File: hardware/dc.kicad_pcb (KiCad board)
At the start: 4 copper layers, 40 x 40 mm, 92 parts, among them J1 DRILL, J2 DRILL, J3 DRILL, J4 DRILL, J5 USB-MINI-B-SMD, J6 STACK-UP-HIGH, J7 STACK-DOWN, J8 STACK-UP-HIGH, J9 STACK-DOWN, P1 black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

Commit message: Add 3d information (tbc); fix direction of some diodes
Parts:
- C1, C12, C13, C14, C16, C17, C18, C19, C2, C20, C22, C24, C25, C9, FB1, FB2, FB3, FB4, FB5: footprint 0402 -> C0402
- C10, C21, C8, L2: footprint 0805 -> C0805
- C11, C15, C23, C5, C6, R9: footprint 0603 -> C0603
- C3, C4: footprint kicad-libraries:ELKO_83 -> ELKO_83
- C7: footprint kicad-libraries:3528-21 -> 3528-21
- D1, D2: footprint kicad-libraries:D0603 -> D0603
- D3, D6, D7, D8, D9: footprint kicad-libraries:SOD-123 -> SOD-123
- D4, D5: footprint kicad-libraries:SOD-128 -> SOD-128
- J5: footprint kicad-libraries:USB-MINI-B-SMD -> USB-MINI-B-SMD
- J6, J8: footprint kicad-libraries:BTB08-ACS-TOP -> BTB08-ACS-TOP
- J7, J9: footprint kicad-libraries:BTB08-ACS-BTM -> BTB08-ACS-BTM
- L1: footprint kicad-libraries:NR3030 -> NR3030
- P1, P2: footprint kicad-libraries:OQ_2P -> OQ_2P
- P3, P4: footprint kicad-libraries:CON-SENSOR -> CON-SENSOR
- Q1, Q2: footprint kicad-libraries:SOIC-8-MOSFET -> SOIC-8-MOSFET
- R1, R10, R11, R12, R13, R15, R18, R2, R3, R4, R5, R6, R7, R8: footprint 0402 -> R0402
- R14: footprint 1206 -> R1206
- R16, R17: footprint 0603 -> R0603
- RP1, RP2, RP3, RP4: footprint kicad-libraries:741X083 -> 4X0402
- SW1, SW2: footprint kicad-libraries:TACT-SWITCH -> TACT-SWITCH
- U1: footprint kicad-libraries:LQFP64 -> LQFP64
- U2: footprint kicad-libraries:PQFN-32 -> PQFN-32
- X1: footprint kicad-libraries:CRYSTAL_3225 -> CRYSTAL_3225
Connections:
- J5 pad 4: (no net) -> Net-(J5-Pad4)
- RP1 pad 2: (no net) -> Net-(RP1-Pad2)
- RP1 pad 3: (no net) -> Net-(RP1-Pad3)
- RP1 pad 6: (no net) -> Net-(RP1-Pad6)
- RP1 pad 7: (no net) -> Net-(RP1-Pad7)
- RP4 pad 6: (no net) -> Net-(RP4-Pad6)
- RP4 pad 7: (no net) -> Net-(RP4-Pad7)
- U1 pad 25: (no net) -> Net-(U1-Pad25)
- U1 pad 31: (no net) -> Net-(U1-Pad31)
- U1 pad 32: (no net) -> Net-(U1-Pad32)
- U1 pad 40: (no net) -> Net-(U1-Pad40)
- U1 pad 50: (no net) -> Net-(U1-Pad50)
- U1 pad 52: (no net) -> Net-(U1-Pad52)
- U2 pad 9: (no net) -> Net-(U2-Pad9)

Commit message: Add 3d information (final)
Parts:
- added REF**: heatsink, kicad-libraries:heatsink, F.Cu at (150.8, 95.0)
- Q3: footprint SOT23GDS -> kicad-libraries:SOT23GDS
- U2: footprint PQFN-32 -> kicad-libraries:PQFN-32

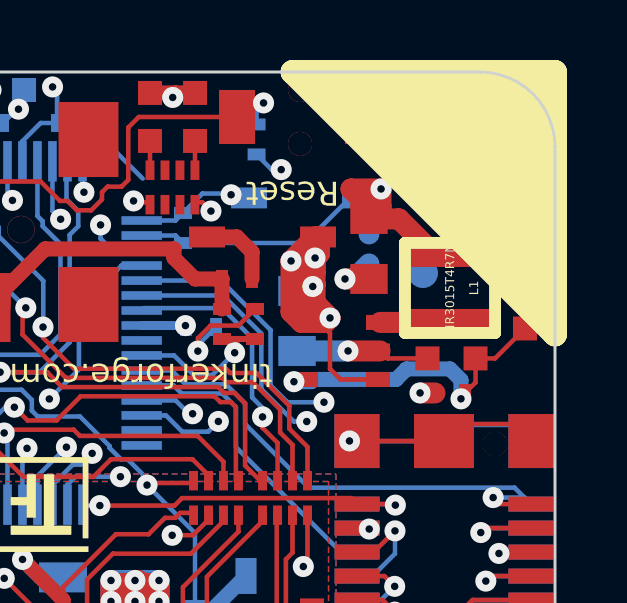
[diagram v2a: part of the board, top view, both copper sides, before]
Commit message: Add 3d component: NR3030
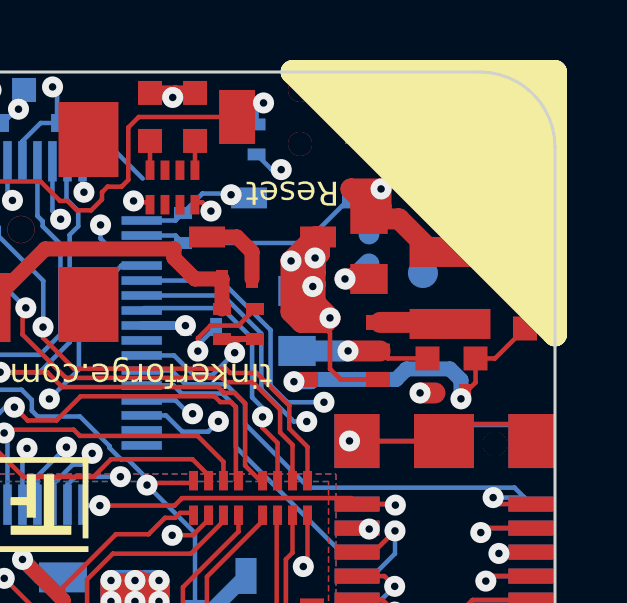
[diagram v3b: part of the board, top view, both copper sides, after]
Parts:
- L1: footprint NR3030 -> kicad-libraries:NR3030
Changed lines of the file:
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@@
     )
-  )
-  (module NR3030 (layer Vorderseite)
-    (at 161.70148 81.54924 90)
-    (attr smd)
-    (fp_text reference L1 (at 0.00254 0.8001 90) (layer F.SilkS)
-      (effects (font (size 0.29972 0.29972) (thickness 0.0762)))
-    )
-    (fp_text value NR3015T4R7M (at 0 0 90) (layer F.SilkS)
-      (effects (font (size 0.29972 0.29972) (thickness 0.0762)))
-    )
-    (fp_line (start -1.50114 -1.50114) (end 1.50114 -1.50114) (layer F.SilkS) (width 0.39878))
-    (fp_line (start 1.50114 -1.50114) (end 1.50114 1.50114) (layer F.SilkS) (width 0.39878))
-    (fp_line (start 1.50114 1.50114) (end -1.50114 1.50114) (layer F.SilkS) (width 0.39878))
-    (fp_line (start -1.50114 1.50114) (end -1.50114 -1.50114) (layer F.SilkS) (width 0.39878))
-    (pad 1 smd rect (at -1.19982 0 90) (size 1 2.70002) (layers Vorderseite F.Paste F.Mask)
-      (net 85 "Net-(L1-Pad1)") (clearance 0.14986))
-    (pad 2 smd rect (at 1.19982 0 90) (size 1 2.70002) (layers Vorderseite F.Paste F.Mask)
-      (net 1 3V3) (clearance 0.14986))
   )
   (module SOT23-5 (layer Vorderseite)
@@
       (scale (xyz 1 1 1))
       (rotate (xyz 0 0 90))
+    )
+  )
+  (module kicad-libraries:NR3030 (layer Vorderseite)
+    (at 161.70148 81.54924 90)
+    (attr smd)
+    (fp_text reference L1 (at 0.00254 0.8001 90) (layer F.Fab)
+      (effects (font (size 0.29972 0.29972) (thickness 0.07493)))
+    )
+    (fp_text value NR3015T4R7M (at 0 0 90) (layer F.Fab)
+      (effects (font (size 0.29972 0.29972) (thickness 0.07493)))
+    )
+    (fp_line (start -1.50114 -1.50114) (end 1.50114 -1.50114) (layer F.Fab) (width 0.39878))
+    (fp_line (start 1.50114 -1.50114) (end 1.50114 1.50114) (layer F.Fab) (width 0.39878))
+    (fp_line (start 1.50114 1.50114) (end -1.50114 1.50114) (layer F.Fab) (width 0.39878))
+    (fp_line (start -1.50114 1.50114) (end -1.50114 -1.50114) (layer F.Fab) (width 0.39878))
+    (pad 1 smd rect (at -1.19982 0 90) (size 1 2.70002) (layers Vorderseite F.Paste F.Mask)
+      (net 85 "Net-(L1-Pad1)") (clearance 0.14986))
+    (pad 2 smd rect (at 1.19982 0 90) (size 1 2.70002) (layers Vorderseite F.Paste F.Mask)
+      (net 1 3V3) (clearance 0.14986))
+    (model Inductors/NR303.wrl
+      (at (xyz 0 0 0.03))
+      (scale (xyz 1 1 1))
+      (rotate (xyz 0 0 90))

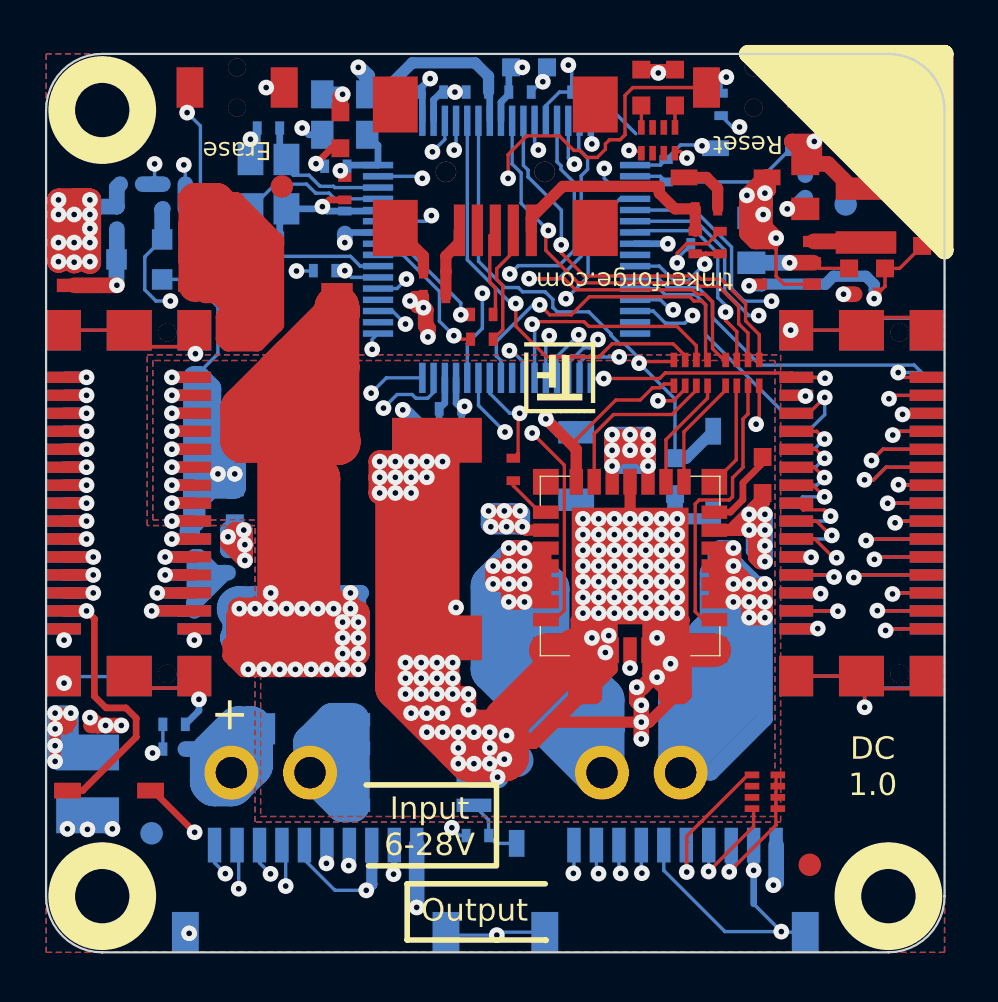
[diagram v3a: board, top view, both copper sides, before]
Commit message: fix partial routing due to footprint size increases
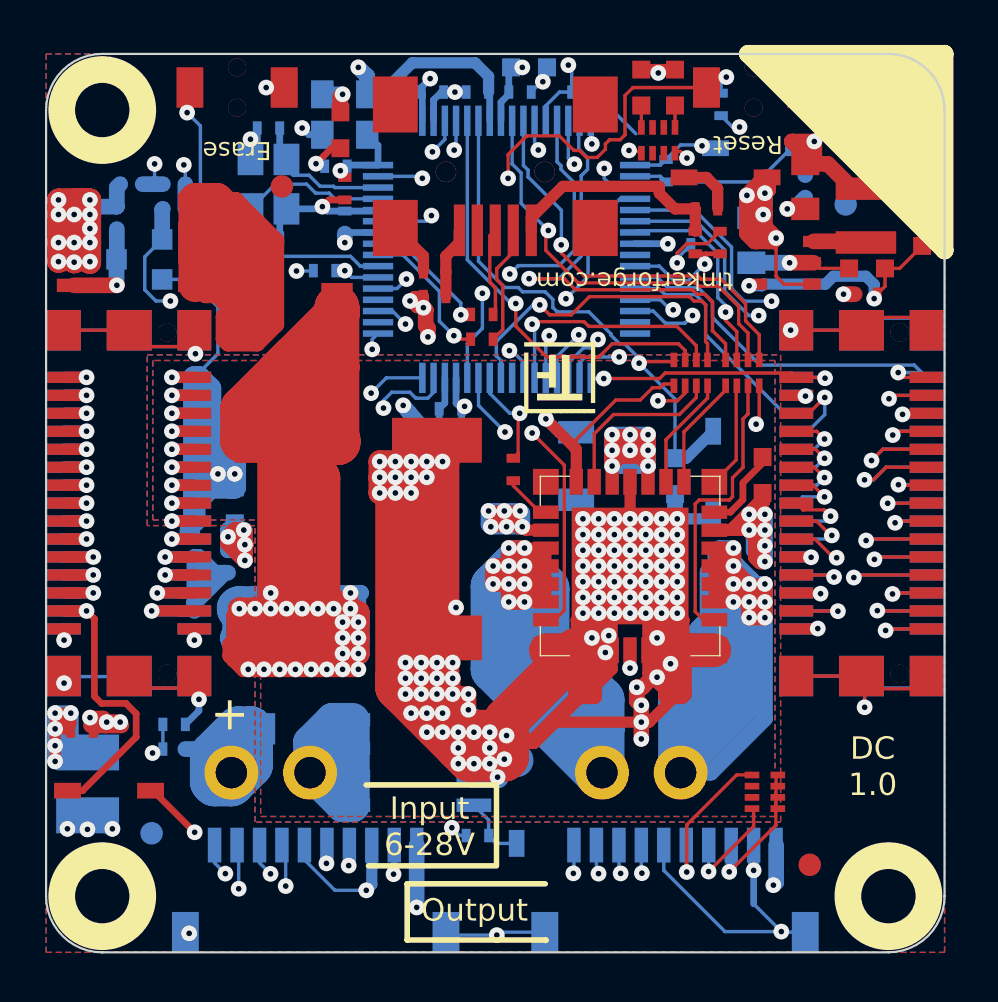
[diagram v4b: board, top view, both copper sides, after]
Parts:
- J1, J2, J3, J4: footprint DRILL_NP -> kicad-libraries:DRILL_NP
- moved FB5 0.27 mm to (126.8, 104.5)
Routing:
- net Net-(FB5-Pad2): track 35.8 -> 37.2 mm

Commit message: dc brick version 1.1
 * fix motor connector position
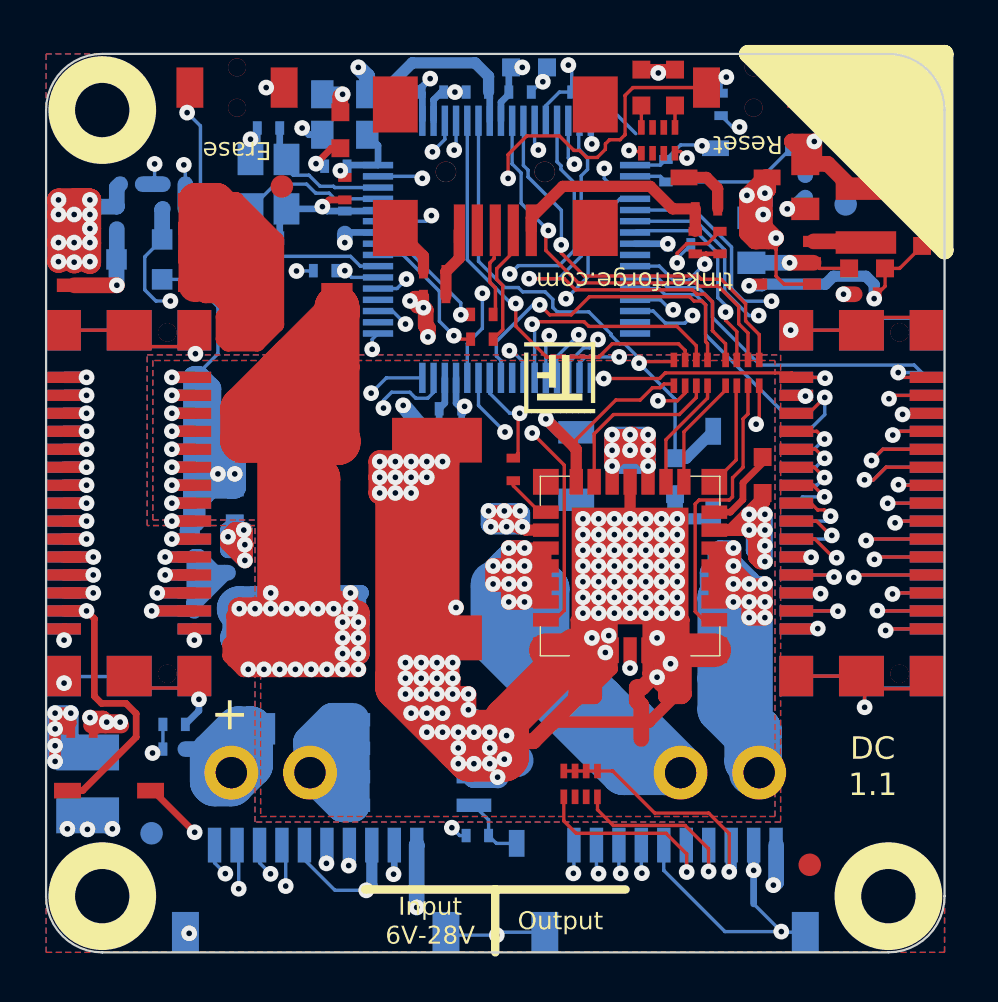
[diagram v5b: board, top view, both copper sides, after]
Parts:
- moved RP4 8.21 mm to (149.0, 106.8), turned to 180 degrees
- moved P2 3.50 mm to (155.2, 106.3)
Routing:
- net Net-(P2-Pad1): track 62.4 -> 73.3 mm
- net 3V3: track 201.4 -> 207.9 mm
- net BRICKLET-I2C-SCL: track 59.2 -> 64.2 mm
- net Net-(P2-Pad2): track 57.0 -> 52.6 mm
- net BRICKLET-I2C-SDA: track 65.2 -> 68.3 mm
- net Net-(FB1-Pad2): track 3.20 -> 3.75 mm
- net STACK-PGND: vias 114 -> 110
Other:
- board text added: "Copyright Tinkerforge GmbH 2017. This documentation describes Open Hardware and is licensed under the CERN OHL v. 1.1. You may redistribute and modify this documentation under the terms of the CERN OHL v.1.1. (http://ohwr.org/cernohl). This documentation is distributed WITHOUT ANY EXPRESS OR IMPLIED WARRANTY, INCLUDING OF MERCHANTABILITY, SATISFACTORY QUALITY AND FITNESS FOR A PARTICULAR PURPOSE.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"
- board text added: "DC 1.1"
- board text added: "Input 6V-28V"
- board text removed: "Copyright Tinkerforge GmbH 2011. This documentation describes Open Hardware and is licensed under the CERN OHL v. 1.1. You may redistribute and modify this documentation under the terms of the CERN OHL v.1.1. (http://ohwr.org/cernohl). This documentation is distributed WITHOUT ANY EXPRESS OR IMPLIED WARRANTY, INCLUDING OF MERCHANTABILITY, SATISFACTORY QUALITY AND FITNESS FOR A PARTICULAR PURPOSE.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"
- board text removed: "DC 1.0"
- board text removed: "Input 6-28V"

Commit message: fix ce and weee logo
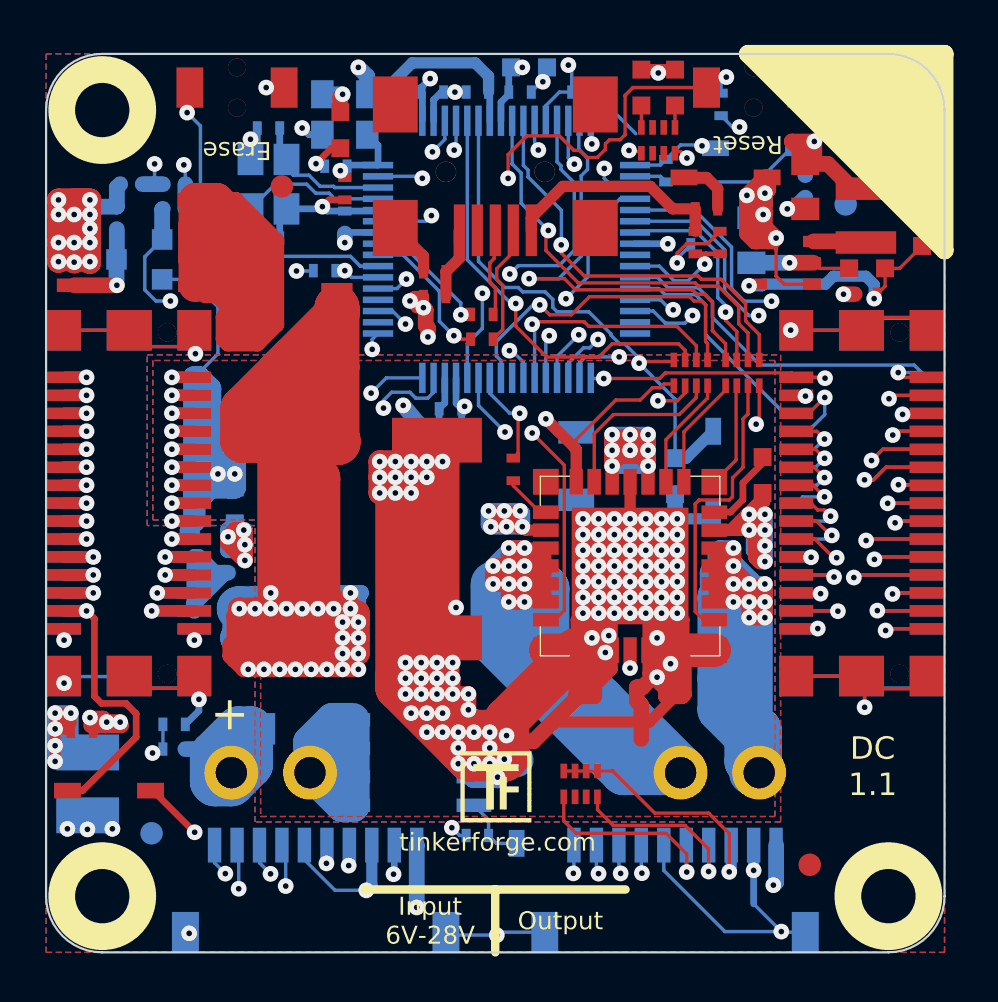
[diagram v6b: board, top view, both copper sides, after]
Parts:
- U1: footprint LQFP64 -> kicad-libraries:LQFP64
- VAL: footprint CE_5mm -> kicad-libraries:CE_5mm
- VAL: footprint WEEE_7mm -> kicad-libraries:WEEE_7mm
- moved Ref** 16.2 mm to (143.7, 105.4), turned to 0 degrees
- turned VAL to 180 degrees

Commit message: Add new 3d model
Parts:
- J6, J8: footprint BTB08-ACS-TOP -> kicad-libraries:BTB08-ACS-TOP
- J7, J9: footprint BTB08-ACS-BTM -> kicad-libraries:BTB08-ACS-BTM
